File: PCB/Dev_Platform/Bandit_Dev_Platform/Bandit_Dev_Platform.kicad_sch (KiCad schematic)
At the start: 8 parts

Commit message: Initial setup for Development Platform
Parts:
- removed C1: 100n, symbol Device:C_Small
- removed U1: ~, symbol BANDIT_PCB_Lib:Raspberry_Pi_Pico
- added C4, C9: 1u, symbol Device:C_Small
- added C5: 10n, symbol Device:C_Small
- added C6, C8: 100n, symbol Device:C_Small
- added D1: LED, symbol Device:LED
- added JP1, JP2, JP3: SolderJumper_2_Open, symbol Jumper:SolderJumper_2_Open
- added P1: USB_C_Plug_USB2.0, symbol Connector:USB_C_Plug_USB2.0
- added R4, R5: 27R, symbol Device:R_Small_US
- added R6: 200R, symbol Device:R_Small_US
- added R7: 10k, symbol Device:R_Small_US
- added R8: 150k, symbol Device:R_Small_US
- added R9: 50k, symbol Device:R_Small_US
- added U1: AD7253, Package_SO:TSSOP-16_4.4x5mm_P0.65mm, symbol BANDIT_PCB_Lib:AD7253
- added U2: RP2040, Package_DFN_QFN:QFN-56-1EP_7x7mm_P0.4mm_EP3.2x3.2mm, symbol MCU_RaspberryPi:RP2040
- added U3: ~, symbol BANDIT_PCB_Lib:AP2210N-4.0TRG1
- added U4: NCP164ASNADJT1G, Package_TO_SOT_SMD:SOT-23-5, symbol BANDIT_PCB_Lib:NCP164ASNADJT1G
- C3: value 10n -> 100n
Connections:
- net +3V3: now also D1.2 (A), JP2.2 (B), U2.1 (IOVDD), U2.10 (IOVDD), U2.22 (IOVDD), U2.33 (IOVDD), U2.42 (IOVDD), U2.44 (VREG_IN), U2.48 (USB_VDD), U2.49 (IOVDD)
- net GND: now also C4.2, C5.2, C6.2, C8.2, C9.2, P1.A1 (GND), P1.A12 (GND), P1.B1 (GND), P1.B12 (GND), P1.S1 (SHIELD), R7.1, R9.1, U1.15 (GND), U2.57 (GND), U3.1 (GND), U4.2 (GND)
- net LED_B: now also U2.17 (GPIO14)
- net LED_G: now also U2.16 (GPIO13)
- net LED_R: now also U2.15 (GPIO12)
- net VBUS: now also C4.1, C5.1, C6.1, P1.A4 (VBUS), P1.A9 (VBUS), P1.B4 (VBUS), P1.B9 (VBUS), U3.3 (VIN), U4.1 (VIN)
- new net: JP1.2 (B), JP2.1 (A), R7.2, U4.3 (EN)
- new net: P1.A6 (D+), R5.1
- new net: P1.A7 (D-), R4.1
- new net: R8.1, R9.2, U4.4 (PG/ADJ)
- new net: D1.1 (K), R6.1
- new net: U2.23 (DVDD), U2.50 (DVDD)
- new net: JP3.2 (B), U3.2 (VOUT)
- new net ADC_CSN: U1.11 (~{CS}), U2.3 (GPIO1)
- new net ADC_SCK: U1.12 (SCLK), U2.4 (GPIO2)
- new net ADC_SDI: U1.10 (SDI), U2.5 (GPIO3)
- new net ADC_SDO_A: U1.13 (SDO_A), U2.6 (GPIO4)
- new net ADC_SDO_B: U1.14 (SDO_B), U2.7 (GPIO5)
- new net USB_D+: R5.2, U2.47 (USB_DP)
- new net USB_D-: R4.2, U2.46 (USB_DM)
- new net USER_LED: R6.2, U2.18 (GPIO15)
- new net VDDA: C8.1, C9.1, JP3.1 (A), R8.2, U1.16 (AVDD), U4.5 (VOUT)
- new net VDDA_EN: JP1.1 (A)
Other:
- note added: "Analog Supply"
- note added: "DNI if tied HIGH"
- note added: "May need RC network SHIELD -> GND if direct tie is issue. Src: FTDI, Microchip, ADI"
- note added: "Note: ADC SPI Dirs From ADC Perspective"
- note added: "PWMs: A[6] (inv) B[6] (inv) A[7] (inv) B[7] (inv)"
- note added: "VEN_IH = 0.7V VEN_IL = 0.2V"
- note added: "Vref_adj = 1.10V Vout = Vfix * (1 + R1 / R2) Note: R1 and R2 should both be < 500k 4.096 = 1.1 * (1 + R1 / 50e3) Pick R2 = 50k R1 = 149,800 ~= 150k"
- note removed: "PWMs: A[1] B[1] A[2]"
- moved on the sheet: D2, R1, R2, R3

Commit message: idk
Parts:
- added R10, R11: 56k, symbol Device:R_Small_US
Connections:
- net GND: now also R10.2, R11.2
- net USB_CC: now reaches P1.A5 (CC)
- net USB_CC: now also R10.1
- net USB_VCONN: now reaches P1.B5 (VCONN)
- net USB_VCONN: now also R11.1
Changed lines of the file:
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@@
+    (stroke (width 0) (type default))
+  )
+  (wire (pts (xy 138.43 46.99) (xy 134.62 46.99))
     (stroke (width 0) (type default))
   )
@@
     (stroke (width 0) (type default))
   )
+  (wire (pts (xy 114.3 46.99) (xy 129.54 46.99))
+    (stroke (width 0) (type default))
+  )
   (wire (pts (xy 208.28 223.52) (xy 189.23 223.52))
     (stroke (width 0) (type default))
@@
     (stroke (width 0) (type default))
   )
+  (wire (pts (xy 58.42 52.07) (xy 69.85 52.07))
+    (stroke (width 0) (type default))
+  )
   (wire (pts (xy 74.93 31.75) (xy 74.93 46.99))
     (stroke (width 0) (type default))
@@
     (stroke (width 0) (type default))
   )
+  (wire (pts (xy 58.42 54.61) (xy 69.85 54.61))
+    (stroke (width 0) (type default))
+  )
   (wire (pts (xy 208.28 218.44) (xy 189.23 218.44))
     (stroke (width 0) (type default))
@@
     (stroke (width 0) (type default))
   )
+  (wire (pts (xy 138.43 33.02) (xy 134.62 33.02))
+    (stroke (width 0) (type default))
+  )
   (wire (pts (xy 200.66 204.47) (xy 208.28 204.47))
     (stroke (width 0) (type default))
@@
     (stroke (width 0) (type default))
   )
+  (wire (pts (xy 138.43 50.8) (xy 138.43 46.99))
+    (stroke (width 0) (type default))
+  )
   (wire (pts (xy 58.42 64.77) (xy 74.93 64.77))
     (stroke (width 0) (type default))
@@
     (stroke (width 0) (type default))
   )
+  (wire (pts (xy 138.43 35.56) (xy 138.43 33.02))
+    (stroke (width 0) (type default))
+  )
   (wire (pts (xy 340.36 46.99) (xy 342.9 46.99))
     (stroke (width 0) (type default))
@@
   )
   (wire (pts (xy 367.03 41.91) (xy 367.03 31.75))
+    (stroke (width 0) (type default))
+  )
+  (wire (pts (xy 114.3 33.02) (xy 129.54 33.02))
     (stroke (width 0) (type default))
   )
@@
     (effects (font (size 1.27 1.27)) (justify left bottom))
   )
+  (label "USB_CC" (at 114.3 33.02 0) (fields_autoplaced)
+    (effects (font (size 1.27 1.27)) (justify left bottom))
+  )
+  (label "USB_VCONN" (at 114.3 46.99 0) (fields_autoplaced)
+    (effects (font (size 1.27 1.27)) (justify left bottom))
+  )
   (label "ADC_SDO_A" (at 189.23 220.98 0) (fields_autoplaced)
     (effects (font (size 1.27 1.27)) (justify left bottom))
@@
     (effects (font (size 1.27 1.27)) (justify right bottom))
   )
+  (label "USB_VCONN" (at 69.85 54.61 180) (fields_autoplaced)
+    (effects (font (size 1.27 1.27)) (justify right bottom))
+  )
   (label "ADC_SDO_B" (at 143.51 196.85 180) (fields_autoplaced)
     (effects (font (size 1.27 1.27)) (justify right bottom))
@@
     (effects (font (size 1.27 1.27)) (justify left bottom))
   )
+  (label "USB_CC" (at 69.85 52.07 180) (fields_autoplaced)
+    (effects (font (size 1.27 1.27)) (justify right bottom))
+  )
   (label "ADC_SDI" (at 189.23 215.9 0) (fields_autoplaced)
     (effects (font (size 1.27 1.27)) (justify left bottom))
@@
   (label "ADC_SDO_A" (at 143.51 194.31 180) (fields_autoplaced)
     (effects (font (size 1.27 1.27)) (justify right bottom))
+  )
+  (symbol (lib_id "Device:R_Small_US") (at 132.08 46.99 90) (unit 1)
+    (in_bom yes) (on_board yes) (dnp no) (fields_autoplaced)
+    (property "Reference" "R11" (at 132.08 40.64 90)
+      (effects (font (size 1.27 1.27)))
+    )
+    (property "Value" "56k" (at 132.08 43.18 90)
+      (effects (font (size 1.27 1.27)))
+    )
+    (property "Footprint" "" (at 132.08 46.99 0)
+      (effects (font (size 1.27 1.27)) hide)
+    )
+    (property "Datasheet" "~" (at 132.08 46.99 0)
+      (effects (font (size 1.27 1.27)) hide)
+    )
+    (pin "1")
+    (pin "2")
+    (instances
+      (project "Bandit_Dev_Platform"
+        (path "/dd3bbd79-e9c1-4976-be4e-f98731bec367"
+          (reference "R11") (unit 1)
+        )
+      )
+    )
+  )
+  (symbol (lib_id "power:GND") (at 138.43 50.8 0) (unit 1)
+    (in_bom yes) (on_board yes) (dnp no) (fields_autoplaced)
+    (property "Reference" "#PWR06" (at 138.43 57.15 0)
+      (effects (font (size 1.27 1.27)) hide)
+    )
+    (property "Value" "GND" (at 138.43 55.88 0)
+      (effects (font (size 1.27 1.27)))
+    )
+    (property "Footprint" "" (at 138.43 50.8 0)
+      (effects (font (size 1.27 1.27)) hide)
+    )
+    (property "Datasheet" "" (at 138.43 50.8 0)
+      (effects (font (size 1.27 1.27)) hide)
+    )
+    (pin "1")
+    (instances
+      (project "Bandit_Dev_Platform"
+        (path "/dd3bbd79-e9c1-4976-be4e-f98731bec367"
+          (reference "#PWR06") (unit 1)
+        )
+      )
+    )
+  )
+  (symbol (lib_id "power:GND") (at 138.43 35.56 0) (unit 1)
+    (in_bom yes) (on_board yes) (dnp no) (fields_autoplaced)
+    (property "Reference" "#PWR020" (at 138.43 41.91 0)
+      (effects (font (size 1.27 1.27)) hide)
+    )
+    (property "Value" "GND" (at 138.43 40.64 0)
+      (effects (font (size 1.27 1.27)))
+    )
+    (property "Footprint" "" (at 138.43 35.56 0)
+      (effects (font (size 1.27 1.27)) hide)
+    )
+    (property "Datasheet" "" (at 138.43 35.56 0)
+      (effects (font (size 1.27 1.27)) hide)
+    )
+    (pin "1")
+    (instances
+      (project "Bandit_Dev_Platform"
+        (path "/dd3bbd79-e9c1-4976-be4e-f98731bec367"
+          (reference "#PWR020") (unit 1)
+        )
+      )
+    )
   )
   (symbol (lib_id "BANDIT_PCB_Lib:AD7253") (at 226.06 204.47 0) (unit 1)
@@
         )
       )
+    )
+  )
+  (symbol (lib_id "Device:R_Small_US") (at 132.08 33.02 90) (unit 1)
+    (in_bom yes) (on_board yes) (dnp no) (fields_autoplaced)
+    (property "Reference" "R10" (at 132.08 26.67 90)
+      (effects (font (size 1.27 1.27)))
+    )
+    (property "Value" "56k" (at 132.08 29.21 90)
+      (effects (font (size 1.27 1.27)))
+    )
+    (property "Footprint" "" (at 132.08 33.02 0)
+      (effects (font (size 1.27 1.27)) hide)
+    )
+    (property "Datasheet" "~" (at 132.08 33.02 0)
+      (effects (font (size 1.27 1.27)) hide)
+    )
+    (pin "1")
+    (pin "2")
+    (instances
+      (project "Bandit_Dev_Platform"
+        (path "/dd3bbd79-e9c1-4976-be4e-f98731bec367"
+          (reference "R10") (unit 1)
+        )
+      )

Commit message: Update dev sch
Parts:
- added C1: 100n, symbol Device:C_Small
- added C10, C7: 15p COG, symbol Device:C_Small
- added C11: 2u2, symbol Device:C_Small
- added J1: Conn_01x03_Pin, symbol Connector:Conn_01x03_Pin
- added R12: 1k, symbol Device:R_Small_US
- added R13: 200R, symbol Device:R_Small_US
- added SW1: SW_SPST, symbol Switch:SW_SPST
- added U5: W25Q32JVSS, Package_SO:SOIC-8_5.23x5.23mm_P1.27mm, symbol Memory_Flash:W25Q32JVSS
- added Y1: 12MHz, symbol Device:Crystal_GND24
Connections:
- net +3V3: now also C1.1, R13.2, U5.8 (VCC)
- net GND: now also U2.19 (TESTEN), C1.2, C10.2, C11.2, C7.1, J1.3 (Pin_3), SW1.2 (B), U5.4 (GND), Y1.2, Y1.4
- net XIN: now reaches U2.20 (XIN)
- net XIN: now also C10.1, Y1.3
- net XOUT: now reaches U2.21 (XOUT)
- net XOUT: now also C7.2, Y1.1
- net at U2.24 (SWCLK): now also J1.1 (Pin_1)
- net at U2.25 (SWD): now also J1.2 (Pin_2)
- net at U2.43 (ADC_AVDD): now also C11.1, R13.1
- net +1V1: now reaches U2.45 (VREG_VOUT)
- net FLASH_IO3: now reaches U2.51 (QSPI_SD3)
- net FLASH_IO3: now also U5.7 (IO3)
- net FLASH_SCK: now reaches U2.52 (QSPI_SCLK)
- net FLASH_SCK: now also U2.56 (QSPI_SS), U5.6 (CLK)
- net FLASH_IO0: now reaches U2.53 (QSPI_SD0)
- net FLASH_IO0: now also U5.5 (DI(IO0))
- net FLASH_IO2: now reaches U2.54 (QSPI_SD2)
- net FLASH_IO2: now also U5.3 (IO2)
- net FLASH_IO1: now reaches U2.55 (QSPI_SD1)
- net FLASH_IO1: now also U5.2 (DO(IO1))
- new net: R12.2, SW1.1 (A)
- new net ~{FLASH_CSN}: R12.1, U5.1 (~{CS})
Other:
- moved on the sheet: U2

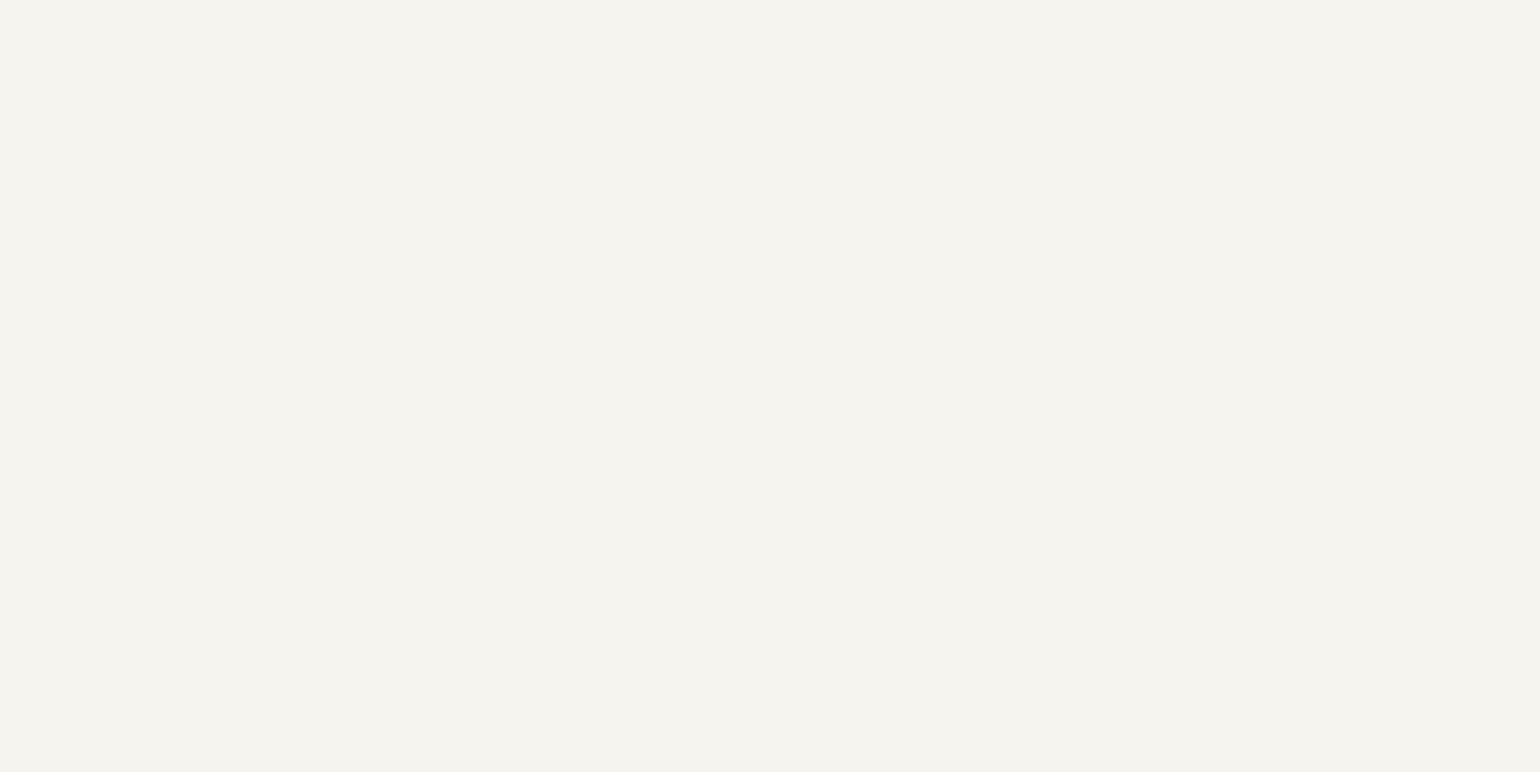
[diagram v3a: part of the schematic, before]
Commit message: Filter added to PCB
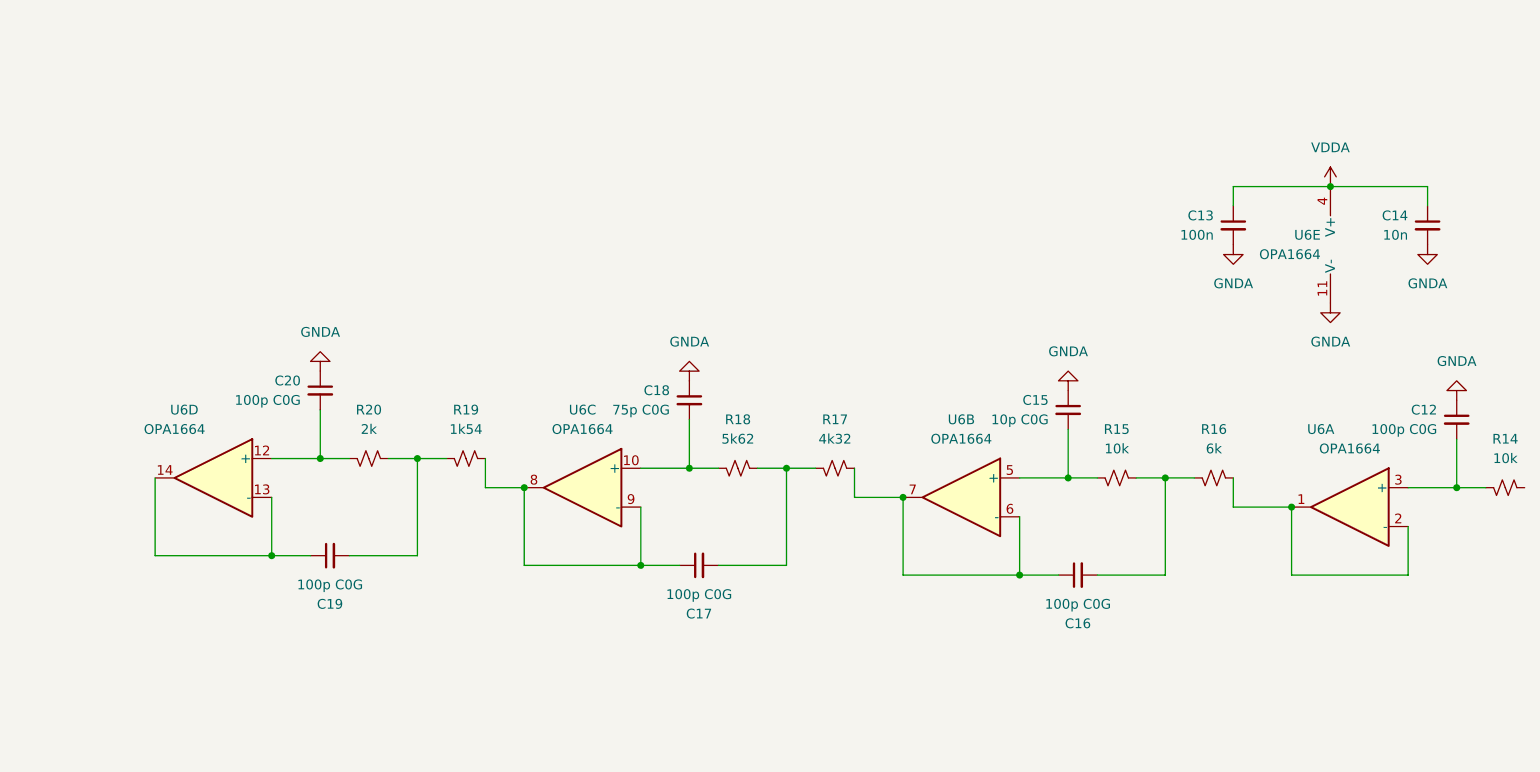
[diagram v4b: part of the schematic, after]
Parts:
- added C12, C16, C17, C19, C20: 100p C0G, symbol Device:C_Small
- added C13: 100n, symbol Device:C_Small
- added C14: 10n, symbol Device:C_Small
- added C15: 10p C0G, symbol Device:C_Small
- added C18: 75p C0G, symbol Device:C_Small
- added R14, R15: 10k, symbol Device:R_Small_US
- added R16: 6k, symbol Device:R_Small_US
- added R17: 4k32, symbol Device:R_Small_US
- added R18: 5k62, symbol Device:R_Small_US
- added R19: 1k54, symbol Device:R_Small_US
- added R20: 2k, symbol Device:R_Small_US
- added U6: OPA1664, symbol Amplifier_Operational:TL074
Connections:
- net VDDA: now also C13.1, C14.1, U6.4 (V+)
- new net: C16.1, R17.1, U6.6 (-), U6.7
- new net: C16.2, R15.1, R16.2
- new net: C12.2, R14.2, U6.3 (+)
- new net: C17.1, R19.1, U6.8, U6.9 (-)
- new net: C17.2, R17.2, R18.1
- new net: C20.2, R20.2, U6.12 (+)
- new net: C19.1, U6.13 (-), U6.14
- new net: C18.2, R18.2, U6.10 (+)
- new net: C19.2, R19.2, R20.1
- new net: C15.2, R15.2, U6.5 (+)
- new net: R16.1, U6.1, U6.2 (-)
- new net GNDA: C12.1, C13.2, C14.2, C15.1, C18.1, C20.1, U6.11 (V-)

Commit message: beep
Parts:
- added C21, C22: 10u, symbol Device:C_Small
- added C23, C24: 36n C0G, symbol Device:C_Small
- added C25: C_Polarized_Small, symbol Device:C_Polarized_Small
- added C26, C28, C31: 100n, symbol Device:C_Small
- added C27, C29, C30: 1u, symbol Device:C_Small
- added C32: 10n C0G, symbol Device:C_Small
- added J2: Conn_Coaxial, symbol Connector:Conn_Coaxial
- added R21, R22, R23, R24: 10R, symbol Device:R_Small_US
- added R25, R26: 50k, symbol Device:R_Small_US
- added R27: 8.06, symbol Device:R_Small_US
- added U7: MCP6S92-E/SN, Package_SO:SOIC-8_3.9x4.9mm_P1.27mm, symbol BANDIT_PCB_Lib:MCP6S92-E/SN
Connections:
- net +3V3: now also U1.9 (DVDD), C28.1, C29.1
- net GND: now also C28.2, C29.2, C32.2
- net GNDA: now also U1.4 (REFGND_A), U1.5 (REFGND_B), C21.2, C22.2, C26.2, C27.2, C30.2, C31.2, R21.1, R24.1, R26.2, U7.4 (VSS)
- net VDDA: now also C26.1, C27.1, C30.1, C31.1, R25.1, U7.8 (VDD)
- net at U1.1 (AINP_A): now also C24.1, R23.2
- net at U1.2 (AINM_A): now also C24.2, R24.2
- net at U1.3 (REFIO_A): now also C22.1
- net at U1.6 (REFIO_B): now also C21.1
- net at U1.7 (AINM_B): now also C23.2, R21.2
- net at U1.8 (AINP_B): now also C23.1, R22.2
- net ~{PGA_CS}: now reaches U2.12 (GPIO9)
- net ~{PGA_CS}: now also U7.5 (~{CS})
- net PGA_SCK: now reaches U2.13 (GPIO10)
- net PGA_SCK: now also U7.7 (SCK)
- net PGA_SI: now reaches U2.14 (GPIO11)
- net PGA_SI: now also U7.6 (SI)
- net PDM_WGN: now reaches U2.29 (GPIO18)
- net PDM_WGN: now also R27.2
- new net: C25.2, R25.2, R26.1, U7.3 (CH1)
- new net: C32.1, R27.1
- new net: C25.1, J2.1 (In)
- new net SE_SIG_A: R23.1
- new net SE_SIG_B: R22.1
- new net SIG_IN: U7.1 (VOUT)
- new net WGN_FB: U7.2 (CH0)
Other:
- note added: "ADC: SPI0 Single SDO or PIO for dual SDO"
- note added: "Could also... like be 10"
- note added: "PGA: SPI1"
- moved on the sheet: C12, C13, C14, C15, C16, C17, C18, C19, C20, R14, R15, R16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

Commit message: Wooooo
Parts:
- removed C16, C17, C19, C20: 100p C0G, symbol Device:C_Small
- removed C18: 75p C0G, symbol Device:C_Small
- removed R14, R15: 10k, symbol Device:R_Small_US
- removed R16: 6k, symbol Device:R_Small_US
- removed R17: 4k32, symbol Device:R_Small_US
- removed R18: 5k62, symbol Device:R_Small_US
- removed R19: 1k54, symbol Device:R_Small_US
- removed R20: 2k, symbol Device:R_Small_US
- removed U6: OPA1664, symbol Amplifier_Operational:TL074
- added C33, C36: 100n, symbol Device:C_Small
- added C34, C37: 2u2, symbol Device:C_Small
- added C35: 10n, symbol Device:C_Small
- added J10, J11, J3, J4, J8: Conn_01x05_Pin, symbol Connector:Conn_01x05_Pin
- added J5, J6: BNC, symbol Connector:Conn_Coaxial
- added J7: SMA, symbol Connector:Conn_Coaxial
- added J9: Conn_01x06_Pin, symbol Connector:Conn_01x06_Pin
- added U6: MCP6486UT-E/OT, Package_TO_SOT_SMD:SOT-23-5, symbol BANDIT_PCB_Lib:MCP6486UT-E/OT
- C12: value 100p C0G -> 100n
- C14: value 10n -> 1u
- C15: value 10p C0G -> 100n
- J2: value Conn_Coaxial -> SMA
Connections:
- net +1V1: now also U2.23 (DVDD), U2.50 (DVDD), C33.1, C34.1
- net +3V3: now also C35.1, C36.1, C37.1, J9.1 (Pin_1)
- net GND: now also C33.2, C34.2, C35.2, C36.2, C37.2, J9.6 (Pin_6)
- net GNDA: now also C12.2, C15.2, J2.2 (Ext), J10.1 (Pin_1), J10.2 (Pin_2), J10.4 (Pin_4), J10.5 (Pin_5), J11.4 (Pin_4), J11.5 (Pin_5), J3.1 (Pin_1), J3.2 (Pin_2), J3.4 (Pin_4), J3.5 (Pin_5), J4.4 (Pin_4), J4.5 (Pin_5), J5.2 (Ext), J6.2 (Ext), J7.2 (Ext), U6.2 (VSS); no longer C12.1, C15.1
- net SE_SIG_A: now also J10.3 (Pin_3)
- net SE_SIG_B: now also J3.3 (Pin_3)
- net SIG_IN: now also J4.3 (Pin_3)
- net VDDA: now also C12.1, C15.1, J11.1 (Pin_1), J11.2 (Pin_2), J4.1 (Pin_1), J4.2 (Pin_2), U6.5 (VDD)
- net at C32.1, R27.1: now also U6.1 (VIN+)
- net at C25.1, J2.1 (In): now also J5.1 (In)
- net at U2.32 (GPIO21): now also J8.1 (Pin_1)
- net at U2.34 (GPIO22): now also J8.2 (Pin_2)
- net at U2.35 (GPIO23): now also J8.3 (Pin_3)
- net at U2.36 (GPIO24): now also J8.4 (Pin_4)
- net at U2.37 (GPIO25): now also J8.5 (Pin_5)
- net at U2.38 (GPIO26_ADC0): now also J9.2 (Pin_2)
- net at U2.39 (GPIO27_ADC1): now also J9.3 (Pin_3)
- net at U2.40 (GPIO28_ADC2): now also J9.4 (Pin_4)
- net at U2.41 (GPIO29_ADC3): now also J9.5 (Pin_5)
- net WGN_FB renamed WGN_OUT
- net WGN_OUT: now also J11.3 (Pin_3), J6.1 (In), J7.1 (In), U6.3 (VIN-), U6.4 (VOUT)
- no-connect marks 0 -> 4
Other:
- note added: "ADC"
- note added: "Channel A (0): Self-Sampling WGN x[n] Channel B (1): SUT Output d[n]"
- note added: "FOR CLIPPY OPTION"
- note added: "PGA INPUT"
- note added: "WGN OUTPUT"
- moved on the sheet: C25, C30, C31, C32, J2, R25, R26, R27, U7

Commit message: Added Filter Round 2
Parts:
- added C1 (x2): 15p C0G, symbol Device:C_Small
- added C2 (x2): 330p C0G, symbol Device:C_Small
- added C3 (x2): 47p C0G, symbol Device:C_Small
- added C4 (x2): 150p C0G, symbol Device:C_Small
- added C5 (x2), C9 (x2): 68p C0G, symbol Device:C_Small
- added C6 (x2): 100p C0G, symbol Device:C_Small
- added C7 (x2): 100n, symbol Device:C_Small
- added C8 (x2): 10n, symbol Device:C_Small
- added R1 (x2): 15k1, symbol Device:R_Small_US
- added R2 (x2): 8k4, symbol Device:R_Small_US
- added R3 (x2): 15k2, symbol Device:R_Small_US
- added R4 (x2): 5k9, symbol Device:R_Small_US
- added R5 (x2): 14k8, symbol Device:R_Small_US
- added R6 (x2): 6k3, symbol Device:R_Small_US
- added R7 (x2): 11k7, symbol Device:R_Small_US
- added U1 (x2): OPA1664, symbol Amplifier_Operational:TL074
- added unit 2 of U1 (x2)
- added unit 5 of U1 (x2)
- added unit 4 of U1 (x2)
- added unit 3 of U1 (x2)
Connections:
- net GNDA: now also C1.1, C1.1, C3.1, C3.1, C5.1, C5.1, C7.2, C7.2, C8.2, C8.2, C9.1, C9.1, U1.11 (V-), U1.11 (V-)
- net SE_SIG_A: now also C2.1, U1.13 (-), U1.14
- net SE_SIG_B: now also C2.1, U1.13 (-), U1.14
- net SIG_IN: now also R7.1
- net VDDA: now also C7.1, C7.1, C8.1, C8.1, U1.4 (V+), U1.4 (V+)
- net WGN_OUT: now also R7.1
- new net: C4.2, R3.1, R4.2 (x2)
- new net: C3.2, R3.2, U1.10 (+) (x2)
- new net: C1.2, R1.2, U1.12 (+) (x2)
- new net: C6.1, R4.1, U1.6 (-), U1.7 (x2)
- new net: C4.1, R2.1, U1.8, U1.9 (-) (x2)
- new net: C2.2, R1.1, R2.2 (x2)
- new net: C5.2, R5.2, U1.5 (+) (x2)
- new net: R6.1, U1.1, U1.2 (-) (x2)
- new net: C9.2, R7.2, U1.3 (+) (x2)
- new net: C6.2, R5.1, R6.2 (x2)
